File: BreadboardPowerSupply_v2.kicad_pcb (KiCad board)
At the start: 2 copper layers, 30.1 x 52.2 mm, 19 parts, among them J1 Barrel_Jack_Switch, J2 Conn_02x02_Odd_Even, J3 Conn_02x02_Odd_Even, SW1 SW_DPDT_x2, U1 LM7805_TO220

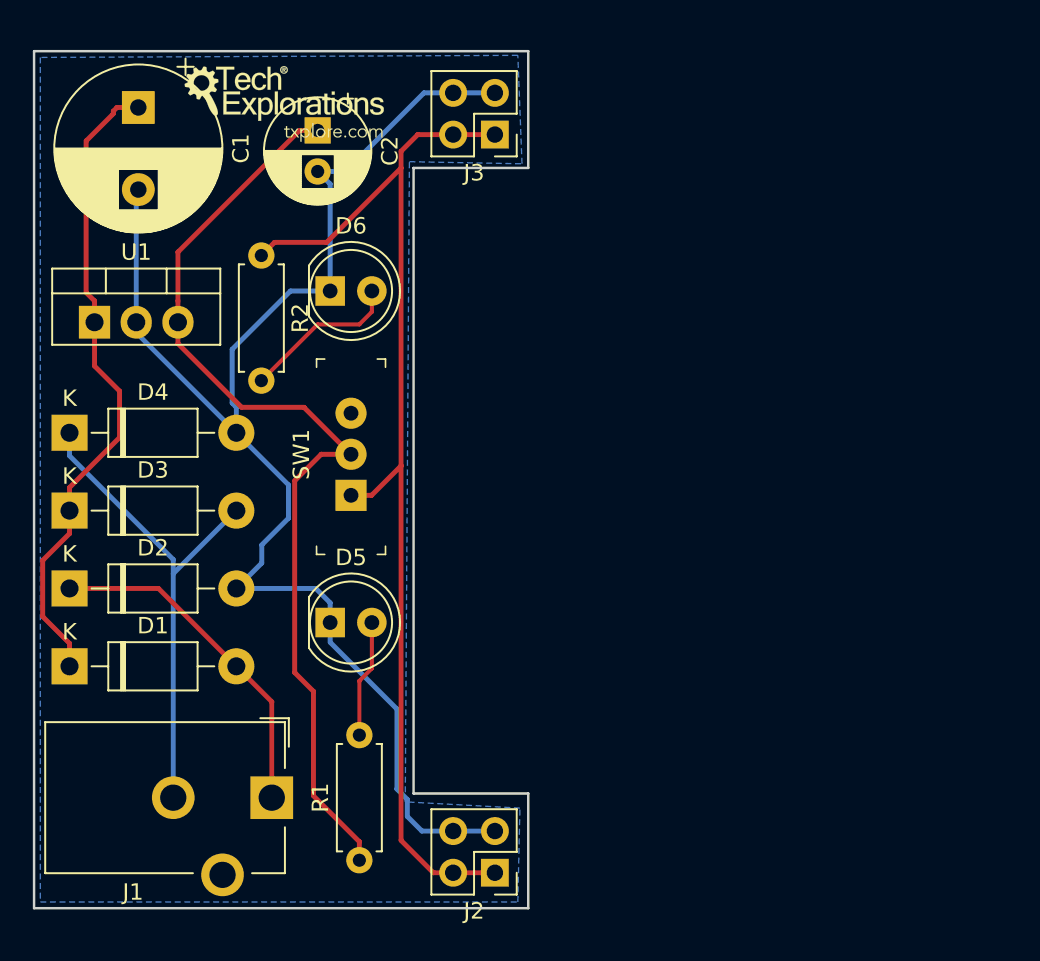
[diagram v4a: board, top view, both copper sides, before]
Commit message: Silkscreen completed.
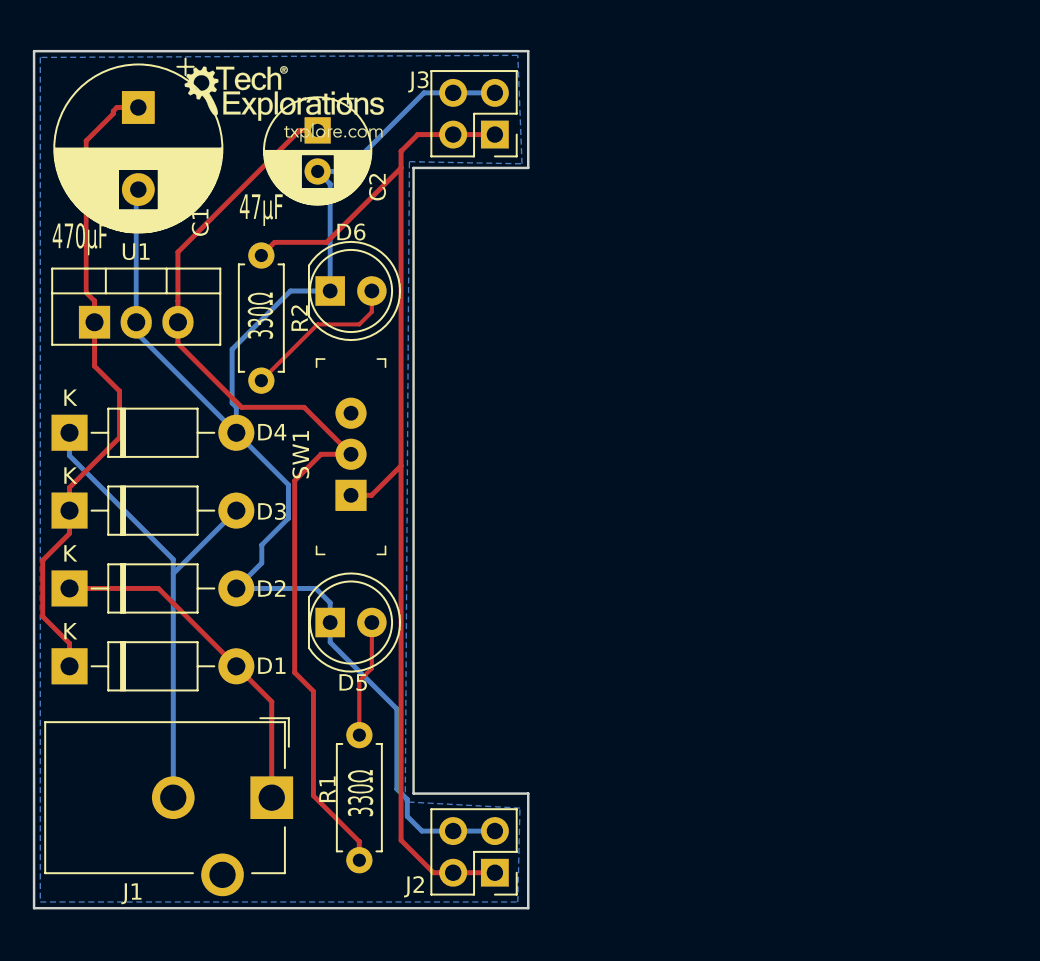
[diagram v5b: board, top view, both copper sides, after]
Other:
- board text added: "330Ω"
- board text added: "470μF"
- board text added: "47μF"
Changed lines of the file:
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@@
   (general
     (thickness 1.6)
-    (drawings 15)
+    (drawings 19)
     (tracks 93)
     (zones 0)
@@
     (34 B.Paste user)
     (35 F.Paste user)
-    (36 B.SilkS user)
+    (36 B.SilkS user hide)
     (37 F.SilkS user)
     (38 B.Mask user)
@@
     (descr "CP, Radial series, Radial, pin pitch=2.50mm, , diameter=6.3mm, Electrolytic Capacitor")
     (tags "CP Radial series Radial pin pitch 2.50mm  diameter 6.3mm Electrolytic Capacitor")
-    (fp_text reference C2 (at 1.25 -4.4 270) (layer F.SilkS)
+    (fp_text reference C2 (at 3.429 -3.683 270) (layer F.SilkS)
       (effects (font (size 1 1) (thickness 0.15)))
     )
@@
     (descr "Diode, DO-41_SOD81 series, Axial, Horizontal, pin pitch=10.16mm, , length*diameter=5.2*2.7mm^2, , http://www.diodes.com/_files/packages/DO-41%20(Plastic).pdf")
     (tags "Diode DO-41_SOD81 series Axial Horizontal pin pitch 10.16mm  length 5.2mm diameter 2.7mm")
-    (fp_text reference D1 (at 5.08 -2.47) (layer F.SilkS)
+    (fp_text reference D1 (at 12.319 0) (layer F.SilkS)
       (effects (font (size 1 1) (thickness 0.15)))
     )
@@
     (descr "Diode, DO-41_SOD81 series, Axial, Horizontal, pin pitch=10.16mm, , length*diameter=5.2*2.7mm^2, , http://www.diodes.com/_files/packages/DO-41%20(Plastic).pdf")
     (tags "Diode DO-41_SOD81 series Axial Horizontal pin pitch 10.16mm  length 5.2mm diameter 2.7mm")
-    (fp_text reference D2 (at 5.08 -2.47) (layer F.SilkS)
+    (fp_text reference D2 (at 12.319 0.042334) (layer F.SilkS)
       (effects (font (size 1 1) (thickness 0.15)))
     )
@@
     (descr "Diode, DO-41_SOD81 series, Axial, Horizontal, pin pitch=10.16mm, , length*diameter=5.2*2.7mm^2, , http://www.diodes.com/_files/packages/DO-41%20(Plastic).pdf")
     (tags "Diode DO-41_SOD81 series Axial Horizontal pin pitch 10.16mm  length 5.2mm diameter 2.7mm")
-    (fp_text reference D3 (at 5.08 -2.47) (layer F.SilkS)
+    (fp_text reference D3 (at 12.319 0.084667) (layer F.SilkS)
       (effects (font (size 1 1) (thickness 0.15)))
     )
@@
     (descr "Diode, DO-41_SOD81 series, Axial, Horizontal, pin pitch=10.16mm, , length*diameter=5.2*2.7mm^2, , http://www.diodes.com/_files/packages/DO-41%20(Plastic).pdf")
     (tags "Diode DO-41_SOD81 series Axial Horizontal pin pitch 10.16mm  length 5.2mm diameter 2.7mm")
-    (fp_text reference D4 (at 5.08 -2.47) (layer F.SilkS)
+    (fp_text reference D4 (at 12.319 0) (layer F.SilkS)
       (effects (font (size 1 1) (thickness 0.15)))
     )
@@
     (descr "LED, diameter 5.0mm, 2 pins, http://cdn-reichelt.de/documents/datenblatt/A500/LL-504BC2E-009.pdf")
     (tags "LED diameter 5.0mm 2 pins")
-    (fp_text reference D5 (at 1.27 -3.96) (layer F.SilkS)
+    (fp_text reference D5 (at 1.397 3.683) (layer F.SilkS)
       (effects (font (size 1 1) (thickness 0.15)))
     )
@@
     (descr "LED, diameter 5.0mm, 2 pins, http://cdn-reichelt.de/documents/datenblatt/A500/LL-504BC2E-009.pdf")
     (tags "LED diameter 5.0mm 2 pins")
-    (fp_text reference D6 (at 1.27 -3.96) (layer F.SilkS)
+    (fp_text reference D6 (at 1.27 -3.556) (layer F.SilkS)
       (effects (font (size 1 1) (thickness 0.15)))
     )
@@
     (descr "Through hole straight pin header, 2x02, 2.54mm pitch, double rows")
     (tags "Through hole pin header THT 2x02 2.54mm double row")
-    (fp_text reference J2 (at 1.27 -2.33 180) (layer F.SilkS)
+    (fp_text reference J2 (at 4.826 -0.762 180) (layer F.SilkS)
       (effects (font (size 1 1) (thickness 0.15)))
     )
@@
     (descr "Through hole straight pin header, 2x02, 2.54mm pitch, double rows")
     (tags "Through hole pin header THT 2x02 2.54mm double row")
-    (fp_text reference J3 (at 1.27 -2.33 180) (layer F.SilkS)
+    (fp_text reference J3 (at 4.572 3.302 180) (layer F.SilkS)
       (effects (font (size 1 1) (thickness 0.15)))
     )
@@
     (descr "Resistor, Axial_DIN0207 series, Axial, Horizontal, pin pitch=7.62mm, 0.25W = 1/4W, length*diameter=6.3*2.5mm^2, http://cdn-reichelt.de/documents/datenblatt/B400/1_4W%23YAG.pdf")
     (tags "Resistor Axial_DIN0207 series Axial Horizontal pin pitch 7.62mm 0.25W = 1/4W length 6.3mm diameter 2.5mm")
-    (fp_text reference R1 (at 3.81 -2.37 90) (layer F.SilkS)
+    (fp_text reference R1 (at 4.318 -1.905 90) (layer F.SilkS)
       (effects (font (size 1 1) (thickness 0.15)))
     )
@@
     (descr "CP, Radial series, Radial, pin pitch=5.00mm, , diameter=10mm, Electrolytic Capacitor")
     (tags "CP Radial series Radial pin pitch 5.00mm  diameter 10mm Electrolytic Capacitor")
-    (fp_text reference C1 (at 2.5 -6.25 270) (layer F.SilkS)
+    (fp_text reference C1 (at 6.985 -3.81 270) (layer F.SilkS)
       (effects (font (size 1 1) (thickness 0.15)))
     )
@@
       (xy -2.549664 -1.91989) (xy -2.469928 -1.911165) (xy -2.400256 -1.919918)) (layer B.SilkS) (width 0.01))
   )
+  (gr_text 330Ω (at 50.8 123.317 90) (layer F.SilkS)
+    (effects (font (size 1.5 0.8) (thickness 0.2)))
+  )
+  (gr_text 47μF (at 50.8 116.713) (layer F.SilkS)
+    (effects (font (size 1.5 0.8) (thickness 0.2)))
+  )
+  (gr_text 470μF (at 39.751 118.491) (layer F.SilkS)
+    (effects (font (size 1.5 0.8) (thickness 0.2)))
+  )
+  (gr_text 330Ω (at 56.896 152.4 90) (layer F.SilkS)
+    (effects (font (size 1.5 0.8) (thickness 0.2)))
+  )
   (gr_text peter@txplore.com (at 51.943 136.271 90) (layer B.SilkS)
